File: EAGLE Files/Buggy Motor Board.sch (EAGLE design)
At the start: 53 parts, among them CON0 M025MM, CON1 M025MM, IC4 4050D, IC5 LP298XS, U1 MCP2551, X1 MICROSD, X2 5566-24, X3 5566-24, Y2 16MHZ

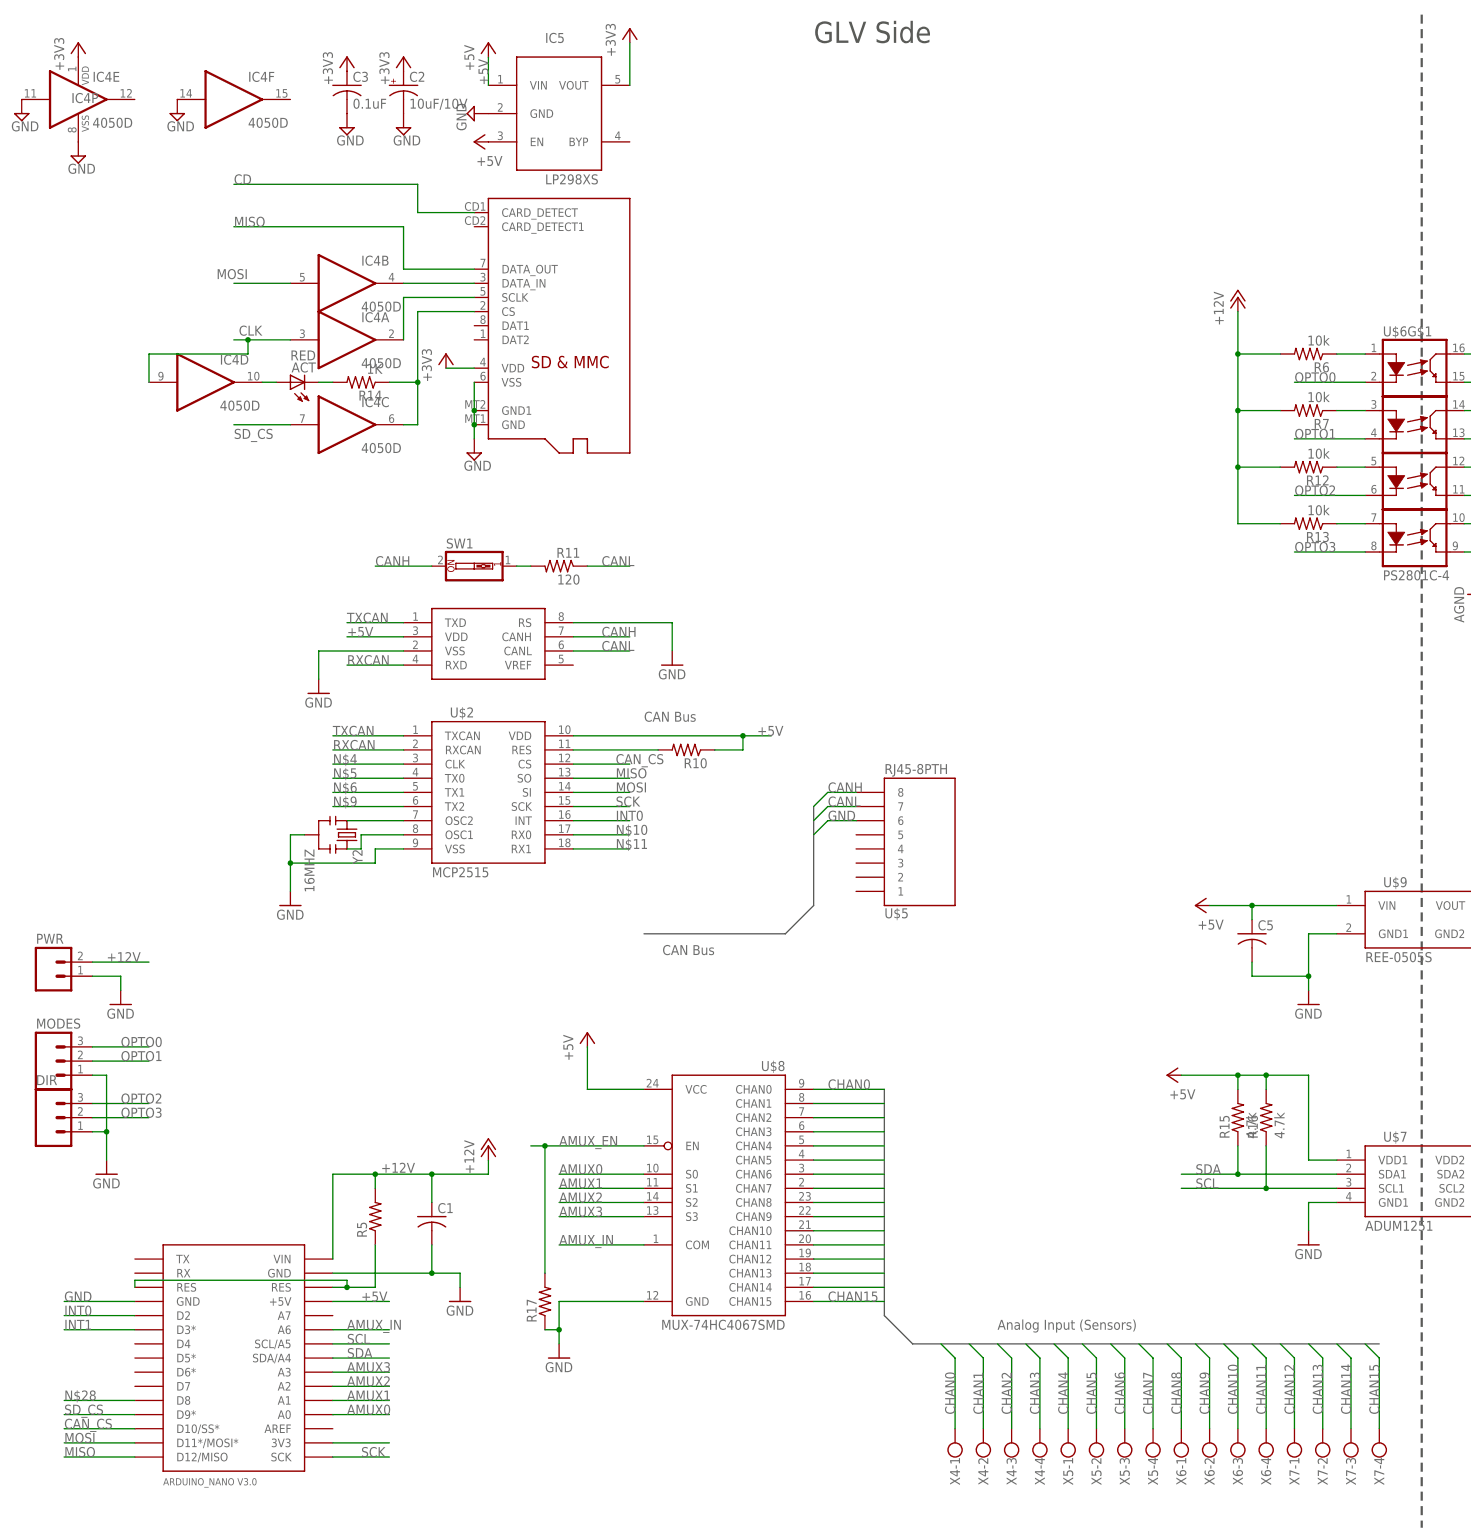
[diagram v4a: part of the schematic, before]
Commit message: Replace Nano with Teensy 3.1
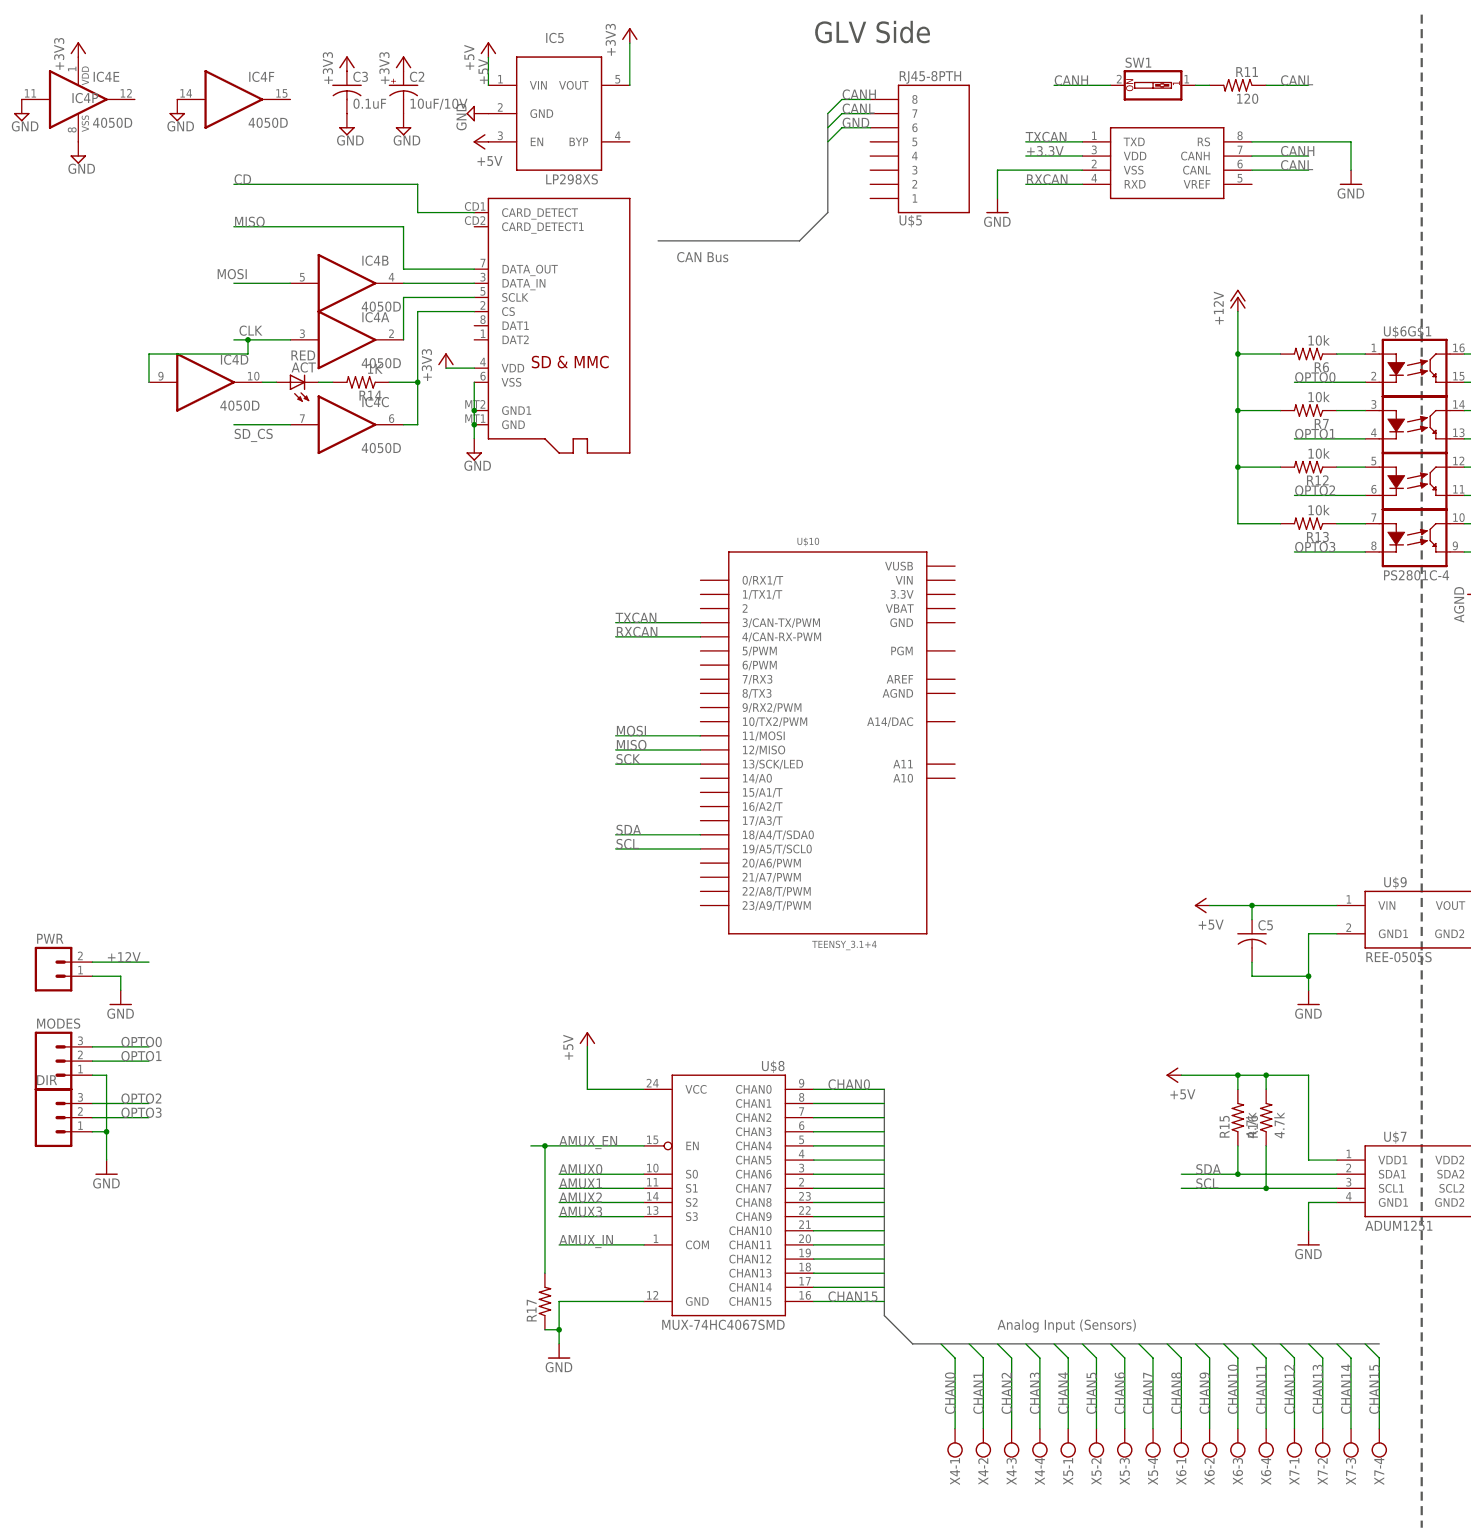
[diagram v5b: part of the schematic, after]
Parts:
- removed C1: (no value), rcl:C-USC1210K
- removed R10, R5: (no value), SparkFun-Resistors:RESISTOR0805-RES
- removed U$1: ARDUINO_NANO, Wetmelon-Boards:ARDUINO_NANO
- removed U$2: MCP2515, Wetmelon-DigitalIC:MCP2515
- removed Y2: 16MHZ, SparkFun-FreqCtrl:RESONATOR16MHZ
- added U$10: TEENSY_3.1+4, Teensy_3_Series_Board_v1.0:TEENSY_3.1+4
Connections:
- removed net CAN_CS: U$1.D10/SS*, U$2.CS
- removed net INT0: U$1.D2, U$2.INT
- removed net INT1: U$1.D3*
- removed net N$1: U$1.3V3
- removed net N$10: U$2.RX0
- removed net N$11: U$2.RX1
- removed net N$14: U$2.OSC2, Y2.1
- removed net N$2: U$2.OSC1, Y2.3
- removed net N$23: R5.1, U$1.RES, U$1.RES@1
- removed net N$28: U$1.D8
- removed net N$3: R10.2, U$2.RES
- removed net N$4: U$2.CLK
- removed net N$5: U$2.TX0
- removed net N$6: U$2.TX1
- removed net N$9: U$2.TX2
- new net +3.3V: U1.VDD
- net +12V: no longer C1.1, R5.2, U$1.VIN
- net +5V: no longer R10.1, U$1.+5V, U$2.VDD, U1.VDD
- net AMUX0: no longer U$1.A0
- net AMUX1: no longer U$1.A1
- net AMUX2: no longer U$1.A2
- net AMUX3: no longer U$1.A3
- net AMUX_IN: no longer U$1.A6
- net GND: no longer C1.2, U$1.GND, U$1.GND@1, U$2.VSS, Y2.2
- net MISO: now also U$10.12/MISO; no longer U$1.D12/MISO, U$2.SO
- net MOSI: now also U$10.11/MOSI; no longer U$1.D11*/MOSI*, U$2.SI
- net RXCAN: now also U$10.4/CAN-RX-PWM; no longer U$2.RXCAN
- net SCK: now also U$10.13/SCK/LED; no longer U$1.SCK, U$2.SCK
- net SCL: now also U$10.19/A5/T/SCL0; no longer U$1.SCL/A5
- net SDA: now also U$10.18/A4/T/SDA0; no longer U$1.SDA/A4
- net SD_CS: no longer U$1.D9*
- net TXCAN: now also U$10.3/CAN-TX/PWM; no longer U$2.TXCAN
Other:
- moved on the sheet: R11, SW1, U$5

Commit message: Add microfit connector
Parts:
- removed X4, X5, X6, X7: (no value), con-wago-500:W237-4
- added U$1: WM9300, Wetmelon-Connectors:WM9300
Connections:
- removed net CLK: IC4A.I, IC4D.I
- new net N$1: U$10.2
- new net N$3: U$10.6/PWM
- new net N$4: U$10.7/RX3
- new net N$5: U$10.8/TX3
- net +5V: no longer U$8.VCC
- net AGND: now also KSI.2; no longer KSI.1
- net AMUX_IN: now also U$10.14/A0
- net CHAN0: now also U$1.P$8; no longer X4-1.KL
- net CHAN1: now also U$1.P$7; no longer X4-2.KL
- net CHAN10: now also U$1.P$11; no longer X6-3.KL
- net CHAN11: now also U$1.P$12; no longer X6-4.KL
- net CHAN12: now also U$1.P$13; no longer X7-1.KL
- net CHAN13: now also U$1.P$14; no longer X7-2.KL
- net CHAN14: now also U$1.P$15; no longer X7-3.KL
- net CHAN15: now also U$1.P$16; no longer X7-4.KL
- net CHAN2: now also U$1.P$6; no longer X4-3.KL
- net CHAN3: now also U$1.P$5; no longer X4-4.KL
- net CHAN4: now also U$1.P$4; no longer X5-1.KL
- net CHAN5: now also U$1.P$3; no longer X5-2.KL
- net CHAN6: now also U$1.P$2; no longer X5-3.KL
- net CHAN7: now also U$1.P$1; no longer X5-4.KL
- net CHAN8: now also U$1.P$9; no longer X6-1.KL
- net CHAN9: now also U$1.P$10; no longer X6-2.KL
- net KSI: now also KSI.1; no longer KSI.2
- net SCK: now also IC4A.I, IC4D.I
- net SD_CS: now also U$10.5/PWM
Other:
- moved on the sheet: KSI, R17, U$8

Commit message: Tweaks
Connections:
- removed net AGND: KSI.2, U$6G$1.L2, U$6G$2.L2, U$6G$3.L2, U$6G$4.L2
- removed net N$3: U$10.6/PWM
- removed net N$4: U$10.7/RX3
- removed net N$5: U$10.8/TX3
- net +3V3: now also R15.2, R16.2, U$10.3.3V, U$10.AREF, U$7.VDD1
- net +5V: now also U$8.VCC; no longer R15.2, R16.2, U$7.VDD1
- net AMUX0: now also U$10.6/PWM
- net AMUX1: now also U$10.7/RX3
- net AMUX2: now also U$10.8/TX3
- net AMUX3: now also U$10.9/RX2/PWM
- net GND1: now also KSI.2, U$6G$1.L2, U$6G$2.L2, U$6G$3.L2, U$6G$4.L2
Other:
- moved on the sheet: IC5

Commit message: Pre-Share Update
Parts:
- removed U1: MCP2551, SparkFun-DigitalIC:MCP2551
- added C1: .33uF, rcl:C-USC0805
- added C6: .1uF, rcl:C-USC0805
- added IC1: (no value), SparkFun-PowerIC:V_REG_78XXSIDE
- added MCP-2562: MCP2562, Wetmelon-DigitalIC:MCP2562
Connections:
- removed net +3.3V: U1.VDD
- removed net N$1: U$10.2
- net +12V: now also C1.1, IC1.IN
- net +3V3: now also MCP-2562.VIO
- net +5V: now also C6.1, IC1.OUT, MCP-2562.VDD, U$10.VIN
- net AMUX_EN: now also U$10.10/TX2/PWM
- net CANH: now also MCP-2562.CANH; no longer U1.CANH
- net CANL: now also MCP-2562.CANL; no longer U1.CANL
- net GND: now also C1.2, C6.2, IC1.GND, MCP-2562.STBY, MCP-2562.VSS, U$10.GND; no longer U1.RS, U1.VSS
- net RXCAN: now also MCP-2562.RXD; no longer U1.RXD
- net TXCAN: now also MCP-2562.TXD; no longer U1.TXD
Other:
- moved on the sheet: IC5, R1, R12, R13, R2, R3, R4, R6, R7, U$6G$1
